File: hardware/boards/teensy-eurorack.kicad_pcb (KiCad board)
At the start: 2 copper layers, 64.8 x 109.2 mm, 52 parts, among them J1 Conn_01x03, J2 Conn_01x02, J27 Conn_01x02, J28 Conn_02x08_Odd_Even, J3 Conn_01x03, U2 AD5754BREZ, U3 AD5754BREZ, U4 Teensy4.1, U5 MCP1700-2502E, U6 AD7606BSTZ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

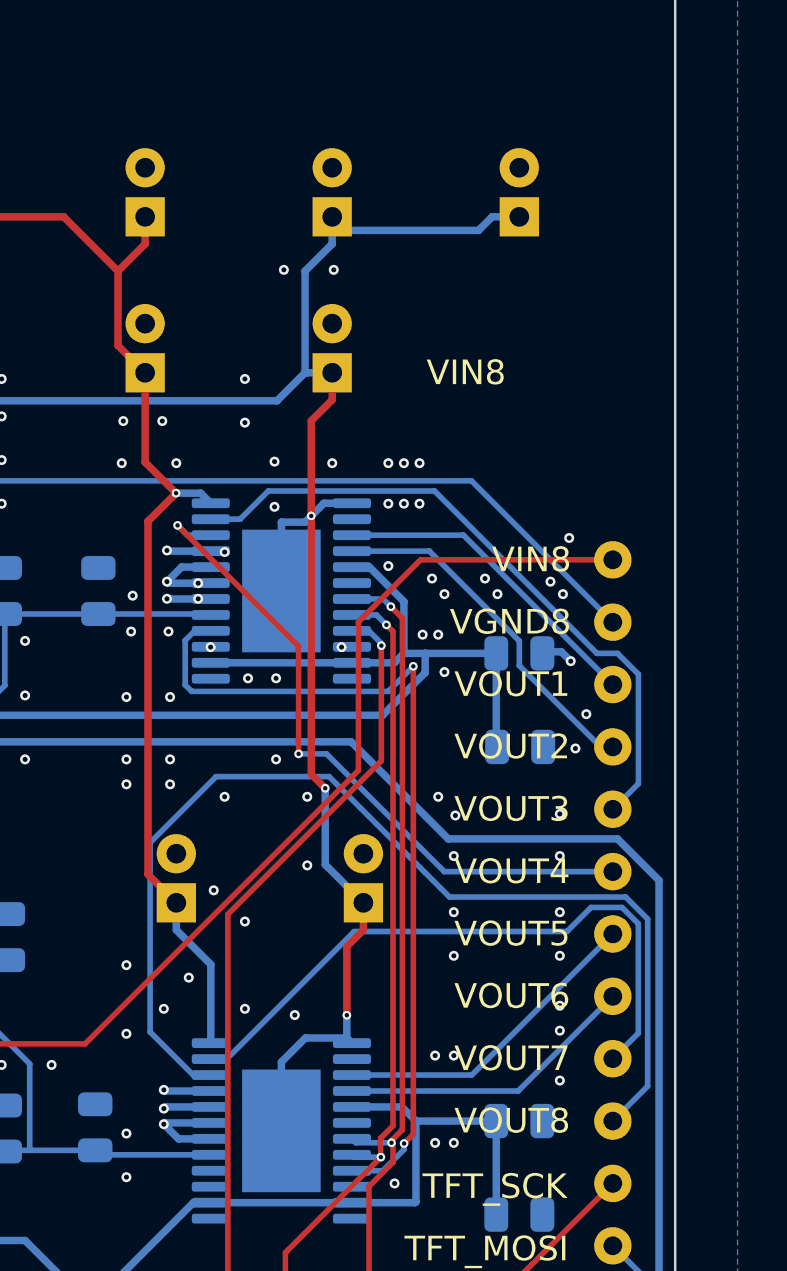
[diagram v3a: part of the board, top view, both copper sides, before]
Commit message: pcb: correction to polarity of bypass caps
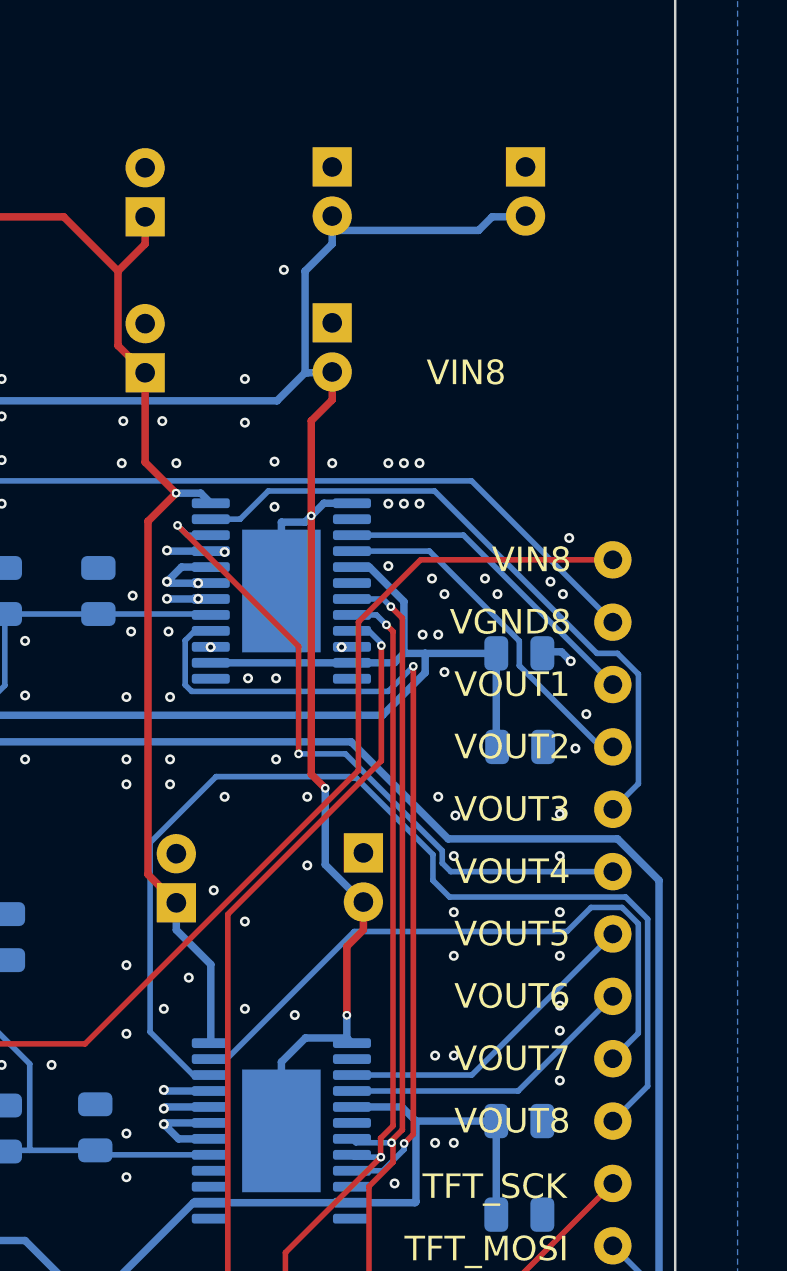
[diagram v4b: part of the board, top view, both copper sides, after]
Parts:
- moved C33 2.05 mm to (166.6, 48.8), turned to 270 degrees
- moved C31 2.03 mm to (158.8, 55.1), turned to 270 degrees
- moved C32 2.03 mm to (160.0, 76.7), turned to 270 degrees
- moved C34 2.03 mm to (158.8, 48.8), turned to 270 degrees
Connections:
- C31 pad 1: -12V -> GND
- C31 pad 2: GND -> -12V
- C32 pad 1: -12V -> GND
- C32 pad 2: GND -> -12V
- C33 pad 1: -12V -> GND
- C33 pad 2: GND -> -12V
- C34 pad 1: -12V -> GND
- C34 pad 2: GND -> -12V
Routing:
- net /VOUT8: track 43.5 -> 44.1 mm
- net GND: vias 464 -> 463
